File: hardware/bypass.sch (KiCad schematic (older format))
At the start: 10 parts, among them Q1 BSS138

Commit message: Remove rescue lib dependency; Join gnd and gnda
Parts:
- removed R10, R11: 100M, symbol R-RESCUE-uMIDI-wah
- added R3, R4: 100M, Resistors_SMD:R_0603, symbol R
- C13: renamed from C49; footprint (none) -> Capacitors_SMD:C_0603; symbol C-RESCUE-uMIDI-wah -> C; Manufacturer (none) -> Murata; Manufacturer Part Number (none) -> GRM188R71E104KA01D; Supplier (none) -> Mouser; Supplier Link (none) -> http://eu.mouser.com/ProductDetail/Murata-Electronics/GRM18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; Supplier Part Number (none) -> 81-GRM39X104K25
- C14: renamed from C50; footprint (none) -> Capacitors_SMD:C_0603; symbol C-RESCUE-uMIDI-wah -> C; Manufacturer (none) -> Murata; Manufacturer Part Number (none) -> GRM188R71E104KA01D; Supplier (none) -> Mouser; Supplier Link (none) -> http://eu.mouser.com/ProductDetail/Murata-Electronics/GRM18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; Supplier Part Number (none) -> 81-GRM39X104K25
- D2: renamed from D3; footprint Diodes_SMD:SOD-323 -> Diodes_SMD:SOD-123; symbol DIODE -> D_Small; Manufacturer (none) -> Diodes Incorporated; Manufacturer Link (none) -> http://www.diodes.com/catalog/Switching_Diodes_5/1N4148W_28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; Manufacturer Part Number (none) -> 1N4148W-7-F; Supplier (none) -> Mouser; Supplier Link (none) -> http://eu.mouser.com/ProductDetail/Diodes-Incorporated/1N41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; Supplier Part Number (none) -> 621-1N4148W-F
- Q1: footprint SOT-23 -> Housings_SOT-23_SOT-143_TSOT-6:SOT-23; Manufacturer (none) -> Fairchild; Manufacturer Part Number (none) -> BSS138; Supplier (none) -> Mouser; Supplier Link (none) -> http://eu.mouser.com/ProductDetail/Fairchild-Semiconductor/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; Supplier Part Number (none) -> 512-BSS138
- R2: renamed from R9; footprint (none) -> Resistors_SMD:R_0603; symbol R-RESCUE-uMIDI-wah -> R; Manufacturer (none) -> Vishay/Dale; Manufacturer Link (none) -> http://www.vishay.com/resistors-fixed/list/product-20011/; Manufacturer Part Number (none) -> CRCW0603100MJPEAHR; Supplier (none) -> Mouser; Supplier Link (none) -> http://eu.mouser.com/ProductDetail/Vishay-Dale/CRCW0603100M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; Supplier Part Number (none) -> 71-CRCW0603100MJPEA
- R5: renamed from R12; footprint (none) -> Resistors_SMD:R_0603; symbol R-RESCUE-uMIDI-wah -> R; Manufacturer (none) -> Vishay/Dale; Manufacturer Link (none) -> http://www.vishay.com/resistors-fixed/list/product-20011/; Manufacturer Part Number (none) -> CRCW0603180RJNEA; Supplier (none) -> Mouser; Supplier Link (none) -> http://www.mouser.de/ProductDetail/Vishay-Dale/CRCW0603180R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; Supplier Part Number (none) -> 71-CRCW0603J-180-E3
- R6: renamed from R13; footprint (none) -> Resistors_SMD:R_0603; symbol R-RESCUE-uMIDI-wah -> R; Manufacturer (none) -> Vishay/Dale; Manufacturer Link (none) -> http://www.vishay.com/resistors-fixed/list/product-20011/; Manufacturer Part Number (none) -> CRCW060310K0JNEA; Supplier (none) -> Mouser; Supplier Link (none) -> http://eu.mouser.com/ProductDetail/Vishay-Dale/CRCW060310K0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; Supplier Part Number (none) -> 71-CRCW0603J-10K-E3
- REL1: value Omron G6K-2G-5VCD -> Omron G6K-2P-5VCD; footprint uMIDI-wah:Omron_G6K-2G -> uMIDI-switcher:Omron_G6K-2P; Manufacturer (none) -> Omron; Manufacturer Part Number (none) -> G6K-2P-Y-DC5; Supplier (none) -> Mouser; Supplier Link (none) -> http://eu.mouser.com/ProductDetail/Omron-Electronics/G6K-2P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; Supplier Part Number (none) -> 653-G6K-2P-Y-DC5
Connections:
- net labels added: bypass, fx_return, fx_send, loop_in, loop_out, relais_n, relais_p
- net labels removed: GNDA
- wire segments 26 -> 29
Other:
- moved on the sheet: Q1

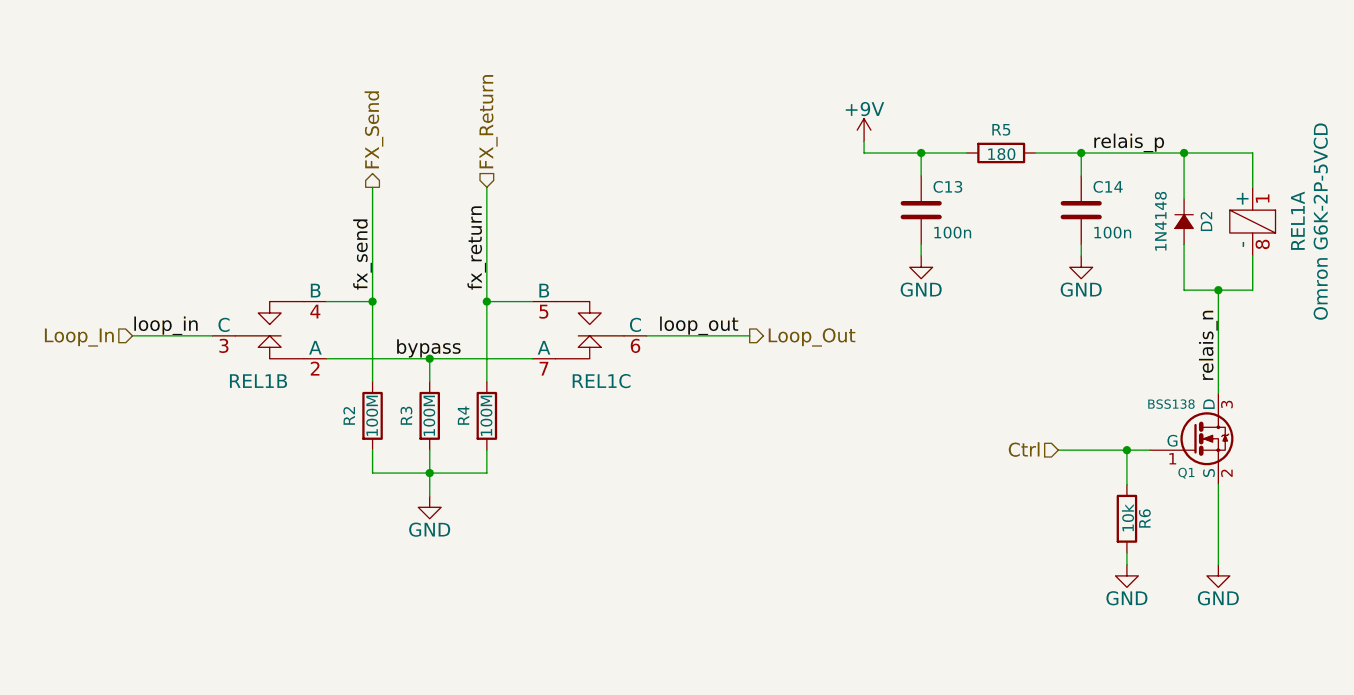
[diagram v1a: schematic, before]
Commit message: Assign remaining footprints
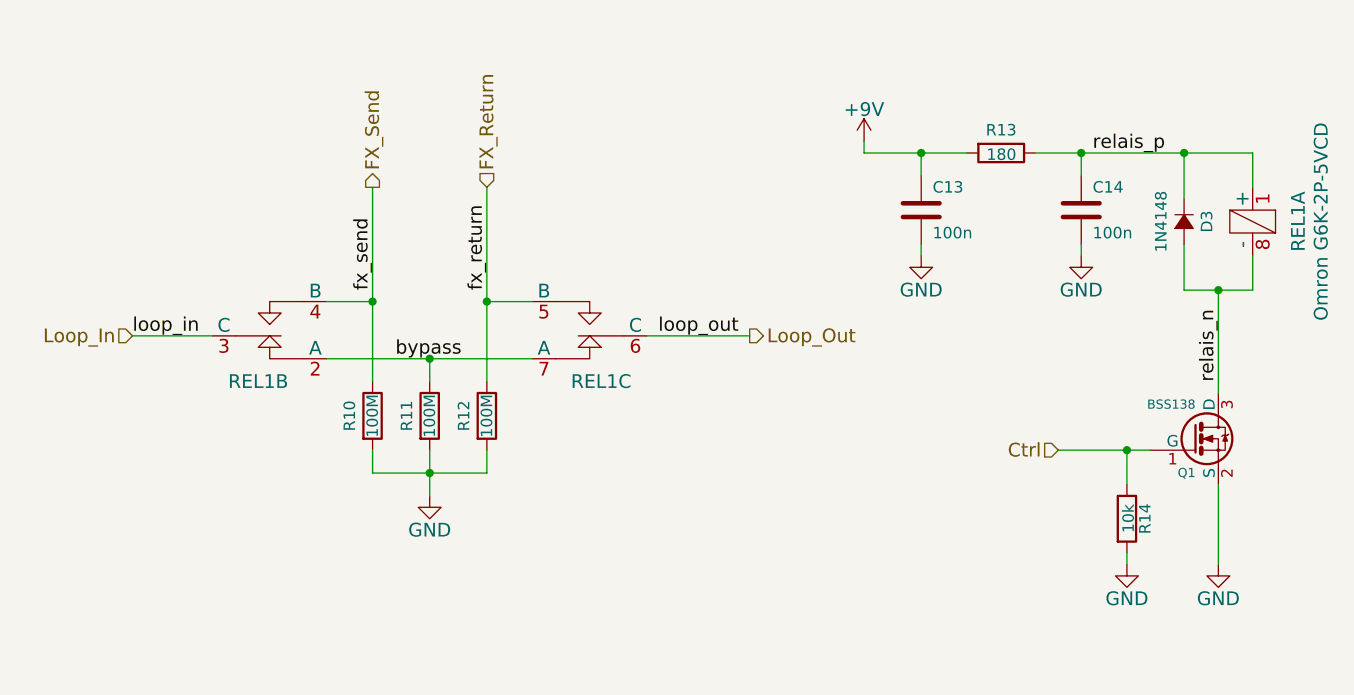
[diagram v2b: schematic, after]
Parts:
- REL1: footprint uMIDI-switcher:Omron_G6K-2P -> uMIDI-wah:Omron_G6K-2P
- renumbered D2 to D3, R2 to R10, R3 to R11, R4 to R12, R5 to R13, R6 to R14

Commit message: Increase pcb size; Add label
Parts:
- REL1: footprint uMIDI-switcher:Omron_G6K-2P -> uMIDI-wah:Omron_G6K-2P
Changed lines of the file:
@@
 F 0 "REL1" H 3700 4000 60  0000 C CNN
 F 1 "Omron G6K-2P-5VCD" H 3700 3500 60  0001 C CNN
-F 2 "uMIDI-switcher:Omron_G6K-2P" H 3700 3800 60  0001 C CNN
+F 2 "uMIDI-wah:Omron_G6K-2P" H 3700 3800 60  0001 C CNN
 F 3 "https://www.omron.com/ecb/products/pdf/en-g6k.pdf" H 3700 4000 60  0001 C CNN
 F 4 "Mouser" H 3700 4000 60  0001 C CNN "Supplier"
@@
 F 0 "REL1" H 5200 4000 60  0000 C CNN
 F 1 "Omron G6K-2P-5VCD" H 4850 4150 60  0001 C CNN
-F 2 "uMIDI-switcher:Omron_G6K-2P" H 5200 3800 60  0001 C CNN
+F 2 "uMIDI-wah:Omron_G6K-2P" H 5200 3800 60  0001 C CNN
 F 3 "https://www.omron.com/ecb/products/pdf/en-g6k.pdf" H 5200 4000 60  0001 C CNN
 F 4 "Mouser" H 5200 4000 60  0001 C CNN "Supplier"
@@
 Connection ~ 7900 3600
 $Comp
-L GND #PWR26
+L GND #PWR021
 U 1 1 54D7A960
 P 7900 4800
-F 0 "#PWR26" H 7900 4550 60  0001 C CNN
+F 0 "#PWR021" H 7900 4550 60  0001 C CNN
 F 1 "GND" H 7900 4650 60  0000 C CNN
 F 2 "" H 7900 4800 60  0000 C CNN
@@
 $EndComp
 $Comp
-L GND #PWR23
+L GND #PWR022
 U 1 1 54D7AB88
 P 6600 3450
-F 0 "#PWR23" H 6600 3200 60  0001 C CNN
+F 0 "#PWR022" H 6600 3200 60  0001 C CNN
 F 1 "GND" H 6600 3300 60  0000 C CNN
 F 2 "" H 6600 3450 60  0000 C CNN
@@
 	7900 4450 7900 4800
 $Comp
-L GND #PWR25
+L GND #PWR023
 U 1 1 54D7B0C5
 P 7500 4800
-F 0 "#PWR25" H 7500 4550 60  0001 C CNN
+F 0 "#PWR023" H 7500 4550 60  0001 C CNN
 F 1 "GND" H 7500 4650 60  0000 C CNN
 F 2 "" H 7500 4800 60  0000 C CNN
@@
 $EndComp
 $Comp
-L GND #PWR24
+L GND #PWR024
 U 1 1 54D7C87A
 P 7300 3450
-F 0 "#PWR24" H 7300 3200 60  0001 C CNN
+F 0 "#PWR024" H 7300 3200 60  0001 C CNN
 F 1 "GND" H 7300 3300 60  0000 C CNN
 F 2 "" H 7300 3450 60  0000 C CNN
@@
 Connection ~ 7300 3000
 $Comp
-L +9V #PWR22
+L +9V #PWR025
 U 1 1 54E940D4
 P 6350 2950
-F 0 "#PWR22" H 6350 2800 60  0001 C CNN
+F 0 "#PWR025" H 6350 2800 60  0001 C CNN
 F 1 "+9V" H 6350 3090 60  0000 C CNN
 F 2 "" H 6350 2950 60  0000 C CNN
@@
 	7900 4050 7900 3600
 $Comp
-L GND #PWR21
+L GND #PWR026
 U 1 1 562E52D6
 P 4450 4500
-F 0 "#PWR21" H 4450 4250 60  0001 C CNN
+F 0 "#PWR026" H 4450 4250 60  0001 C CNN
 F 1 "GND" H 4450 4350 60  0000 C CNN
 F 2 "" H 4450 4500 60  0000 C CNN
